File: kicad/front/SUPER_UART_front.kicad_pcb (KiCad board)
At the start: 2 copper layers, 100 x 43 mm, 253 parts, among them CON2 PIN-2x3, CON3 RS232, CON4 PORT D, CON5 PORT D, CON6 PORT B, CON7 PORT A, CON8 PORT C, Q1 PDTA143ZT, Q10 2N7002PS, Q11 N-MOS_small, Q12 PDTA143ZT, Q13 N-MOS_small, Q14 N-MOS_small, Q2 PDTA143ZT, Q3 N-MOS_small, Q4 PDTA143ZT, Q5 2N7002PS, Q6 N-MOS_small, Q7 PDTA143ZT, Q8 N-MOS_small, Q9 PDTA143ZT, SW1 5V_1, SW10 3V3_2, SW11 2V5_2, SW12 1V8_2, SW13 I2C_A, SW14 SPI_A, SW15 I2C_B, SW16 SPI_B, SW17 BOOT, SW18 DTR, SW19 RTS, SW2 3V3_1, SW3 2V5_1, SW4 1V8_1, SW5 RX, SW6 TX, SW7 SPY, SW8 ISO, SW9 5V_2, U1 STM32F030C6T6, U10 LP2951CD, U11 74HC595D, U12 74LVC8T245PW, U13 74LVC2T45DCU, U14 74LVC1T45GW, U15 74LVC1T45GW, U16 LP2951CD, U2 MIC5504-3.3YM5-TR, U4 74HC08P, U5 MAX3243EIPW, U6 74HC08P, U7 74LVC8T245PW, U8 74LVC8T245PW, U9 74LVC1T45GW

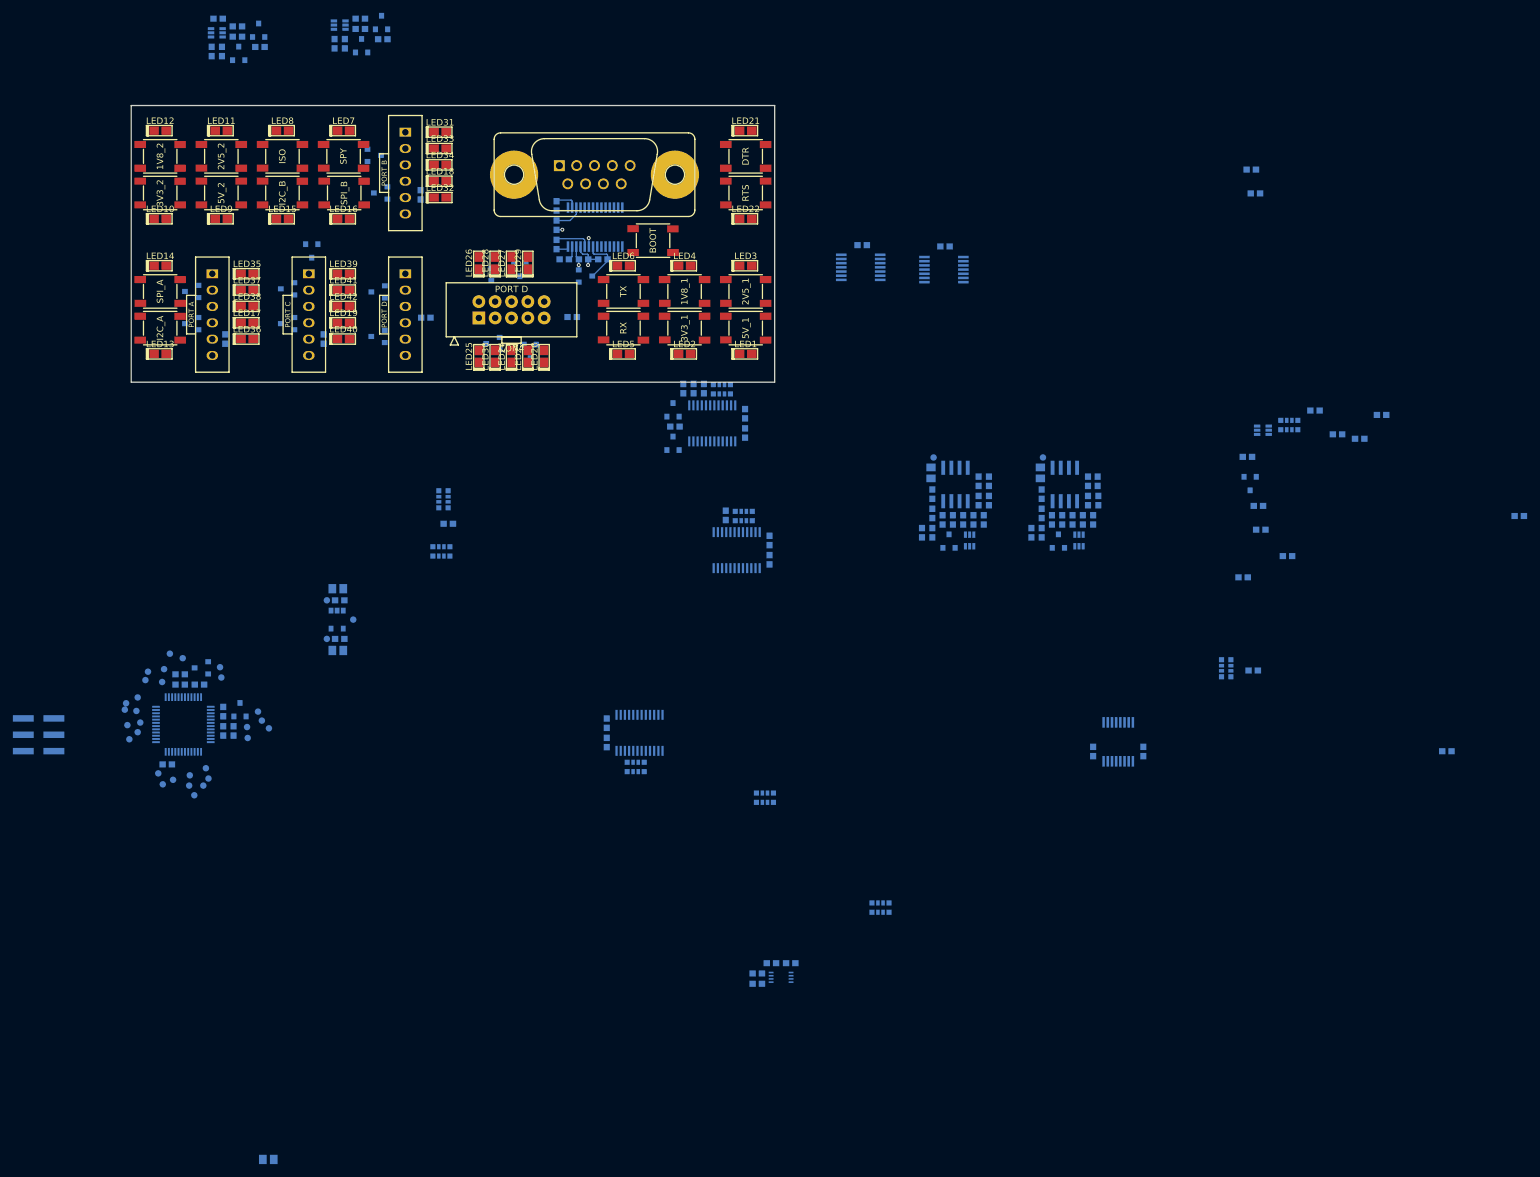
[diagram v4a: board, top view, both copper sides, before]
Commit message: Routing before moving to 4 layers
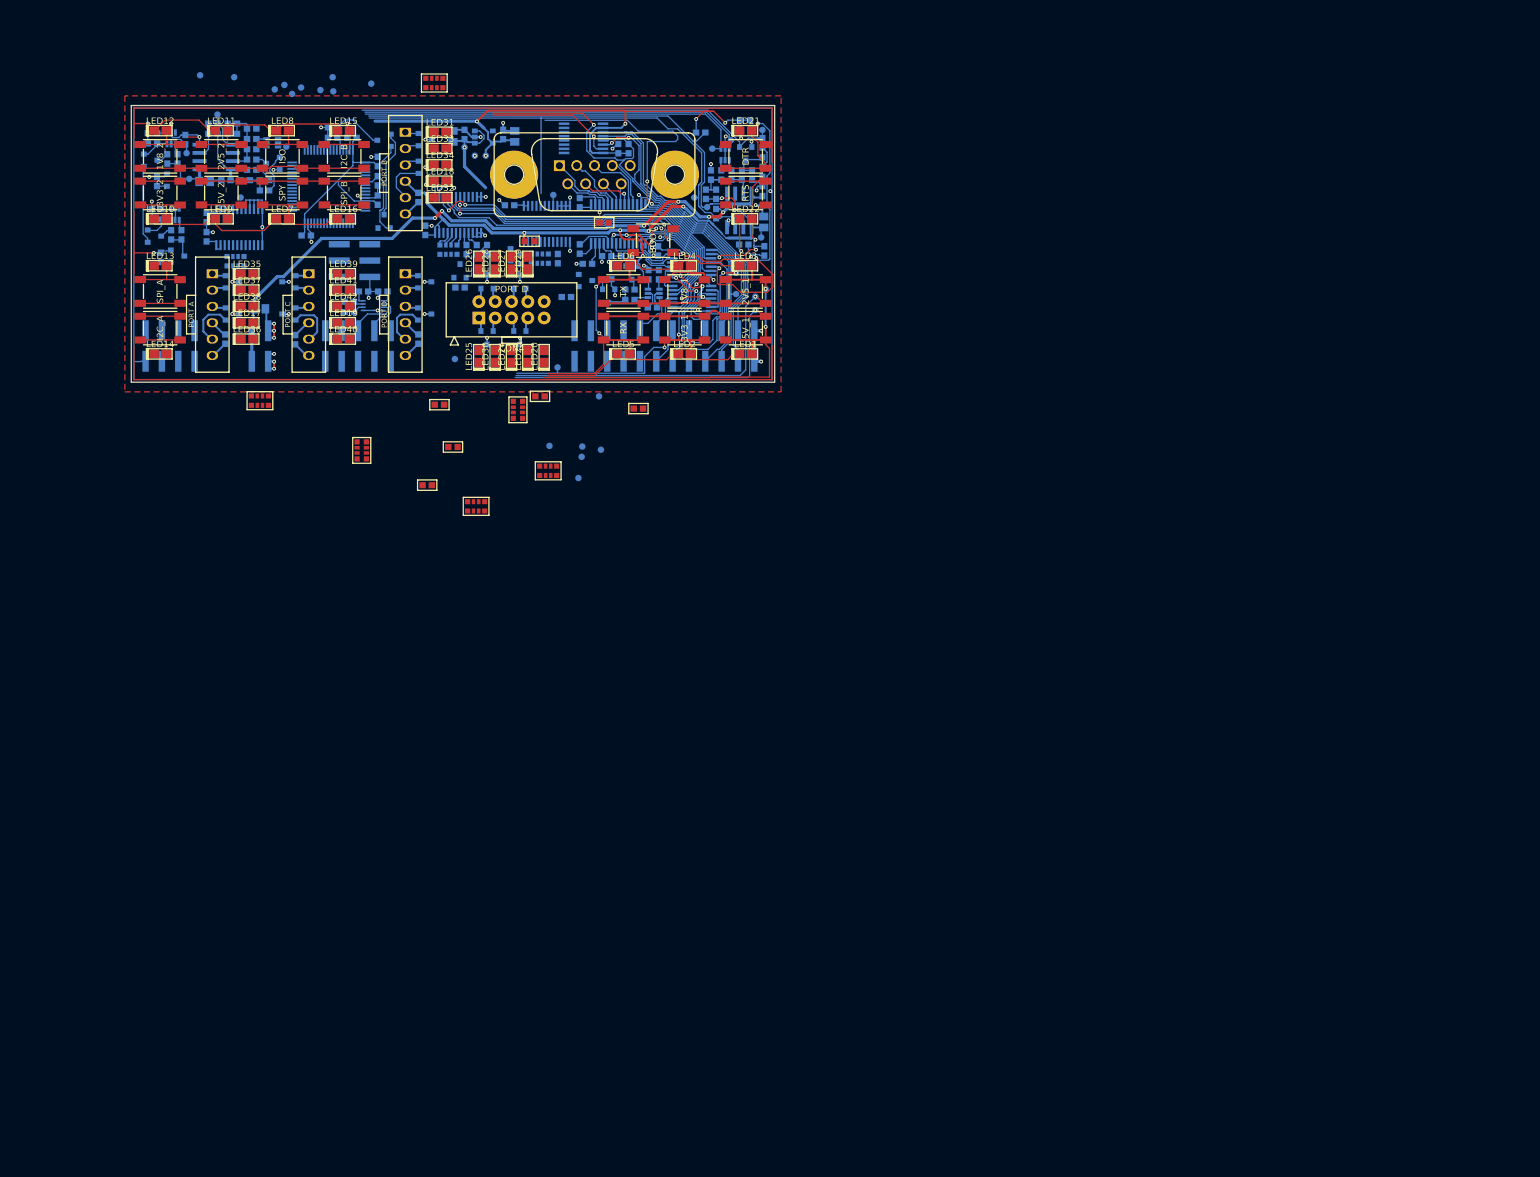
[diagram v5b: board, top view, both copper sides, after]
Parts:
- added CON1: PIN-2x4, pnPinheaders:PIN4x2SMD, B.Cu at (26.0, 55.9)
- added CON10: PIN-2x5, pnPinheaders:PIN5x2SMD, B.Cu at (55.2, 55.9)
- added CON11: PIN-2x12, pnPinheaders:PIN12x2SMD, B.Cu at (102.9, 55.9)
- added CON9: PIN-2x2, pnPinheaders:PIN2x2SMD, B.Cu at (40.0, 55.9)
- added TP36: Testpoint, pnConnector:TP_1mm, B.Cu at (42.3, 16.0)
- added TP37: Testpoint, pnConnector:TP_1mm, B.Cu at (43.8, 15.3)
- added TP38: Testpoint, pnConnector:TP_1mm, B.Cu at (45.0, 16.7)
- added TP39: Testpoint, pnConnector:TP_1mm, B.Cu at (51.4, 16.3)
- C15, C18, C21, R1, R14, R7, R8, RN1, RN2, RN3, RN6, RN8, RN9: moved to F.Cu
- U1: value STM32F030C6T6 -> STM32F030R8T6; footprint ST_LQFP48_ST_default -> niceSemiconductors:QFP-64-0.5_N
- moved R37 148.3 mm to (32.7, 21.3), turned to 180 degrees
- moved C43 146.8 mm to (35.7, 21.3), turned to 0 degrees
- moved R38 146.3 mm to (32.7, 22.9), turned to 0 degrees
- moved R40 144.7 mm to (35.7, 22.9), turned to 180 degrees
- moved R45 144.2 mm to (38.7, 22.1), turned to 180 degrees
- moved RN6 143.1 mm to (67.1, 15.0)
- moved R44 142.1 mm to (38.7, 23.7), turned to 180 degrees
- moved U16 141.4 mm to (33.2, 26.5), turned to 90 degrees
- moved C30 140.4 mm to (100.4, 44.8), turned to 90 degrees
- moved R43 140.0 mm to (38.7, 25.3), turned to 180 degrees
- moved Q10 139.8 mm to (41.9, 24.3), turned to 270 degrees
- moved TP35 139.6 mm to (29.0, 29.9), turned to 90 degrees
- moved R42 137.9 mm to (38.7, 26.9), turned to 180 degrees
- moved C44 137.6 mm to (31.4, 30.3), turned to 0 degrees
- moved R7 136.1 mm to (67.9, 65.0)
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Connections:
- net /CTS_A  renamed /CTS_A
- net /CTS_B  renamed /CTS_B
- net /CTS_C  renamed /CTS_C
- net /DTR_A  renamed /DTR_A
- net /DTR_B  renamed /DTR_B
- net /DTR_C  renamed /DTR_C
- net /RI_D  renamed /RI_D
- D10 pad 1: /SUPER_UART_front_UART234/DTR_A_VDD2 -> /SUPER_UART_front_UART234/RXD_A_VDD2
- D10 pad 2: /SUPER_UART_front_UART234/TXD_A_VDD2 -> /SUPER_UART_front_UART234/DTR_A_VDD2
- D11 pad 1: /SUPER_UART_front_UART234/RXD_A_VDD2 -> /SUPER_UART_front_UART234/CTS_A_VDD2
- D11 pad 2: /SUPER_UART_front_UART234/CTS_A_VDD2 -> /SUPER_UART_front_UART234/TXD_A_VDD2
- D12 pad 2: /SUPER_UART_front_UART234/TXD_C_VDD2 -> /SUPER_UART_front_UART234/RXD_C_VDD2
- D13 pad 1: /SUPER_UART_front_UART234/RXD_C_VDD2 -> /SUPER_UART_front_UART234/TXD_C_VDD2
- D6 pad 1: /SUPER_UART_front_UART1/DTR_D_VDD1 -> /SUPER_UART_front_UART1/CTS_D_VDD1
- D7 pad 2: /SUPER_UART_front_UART1/CTS_D_VDD1 -> /SUPER_UART_front_UART1/DTR_D_VDD1
- D8 pad 1: /SUPER_UART_front_UART1/DTR_B_VDD1 -> /SUPER_UART_front_UART1/CTS_B_VDD1
- D9 pad 2: /SUPER_UART_front_UART1/CTS_B_VDD1 -> /SUPER_UART_front_UART1/DTR_B_VDD1
- LED1 pad 1: /SUPER_UART_front_uC/COL1 -> /SUPER_UART_front_uC/COL3
- LED1 pad 2: /SUPER_UART_front_uC/LED1 -> /SUPER_UART_front_uC/LED2
- LED10 pad 1: /SUPER_UART_front_uC/COL2 -> /SUPER_UART_front_uC/COL4
- LED10 pad 2: /SUPER_UART_front_uC/LED3 -> /SUPER_UART_front_uC/LED4
- LED13 pad 1: /SUPER_UART_front_uC/COL1 -> /SUPER_UART_front_uC/COL4
- LED13 pad 2: /SUPER_UART_front_uC/LED4 -> /SUPER_UART_front_uC/LED1
- LED14 pad 1: /SUPER_UART_front_uC/COL2 -> /SUPER_UART_front_uC/COL4
- LED14 pad 2: /SUPER_UART_front_uC/LED4 -> /SUPER_UART_front_uC/LED2
- LED15 pad 1: /SUPER_UART_front_uC/COL3 -> /SUPER_UART_front_uC/COL1
- LED15 pad 2: /SUPER_UART_front_uC/LED4 -> /SUPER_UART_front_uC/LED3
- LED16 pad 1: /SUPER_UART_front_uC/COL4 -> /SUPER_UART_front_uC/COL1
- LED2 pad 2: /SUPER_UART_front_uC/LED1 -> /SUPER_UART_front_uC/LED2
- LED4 pad 1: /SUPER_UART_front_uC/COL4 -> /SUPER_UART_front_uC/COL2
- LED6 pad 1: /SUPER_UART_front_uC/COL2 -> /SUPER_UART_front_uC/COL1
- LED6 pad 2: /SUPER_UART_front_uC/LED2 -> /SUPER_UART_front_uC/LED1
- LED7 pad 1: /SUPER_UART_front_uC/COL3 -> /SUPER_UART_front_uC/COL2
- LED7 pad 2: /SUPER_UART_front_uC/LED2 -> /SUPER_UART_front_uC/LED4
- LED8 pad 1: /SUPER_UART_front_uC/COL4 -> /SUPER_UART_front_uC/COL2
- LED8 pad 2: /SUPER_UART_front_uC/LED2 -> /SUPER_UART_front_uC/LED3
- LED9 pad 1: /SUPER_UART_front_uC/COL1 -> /SUPER_UART_front_uC/COL3
- LED9 pad 2: /SUPER_UART_front_uC/LED3 -> /SUPER_UART_front_uC/LED4
- RN3 pad 5: /DCD_D  -> /DCD_D
- RN3 pad 6: /DSR_D  -> /DSR_D
- RN3 pad 7: /CTS_D  -> /CTS_D
- SW1 pad 1: /SUPER_UART_front_uC/SW1 -> /SUPER_UART_front_uC/SW2
- SW1 pad 2: /SUPER_UART_front_uC/COL1 -> /SUPER_UART_front_uC/COL3
- SW10 pad 1: /SUPER_UART_front_uC/SW3 -> /SUPER_UART_front_uC/SW4
- SW10 pad 2: /SUPER_UART_front_uC/COL2 -> /SUPER_UART_front_uC/COL4
- SW13 pad 1: /SUPER_UART_front_uC/SW4 -> /SUPER_UART_front_uC/SW1
- SW13 pad 2: /SUPER_UART_front_uC/COL1 -> /SUPER_UART_front_uC/COL4
- SW14 pad 1: /SUPER_UART_front_uC/SW4 -> /SUPER_UART_front_uC/SW2
- SW14 pad 2: /SUPER_UART_front_uC/COL2 -> /SUPER_UART_front_uC/COL4
- SW15 pad 1: /SUPER_UART_front_uC/SW4 -> /SUPER_UART_front_uC/SW3
- SW15 pad 2: /SUPER_UART_front_uC/COL3 -> /SUPER_UART_front_uC/COL1
- SW16 pad 2: /SUPER_UART_front_uC/COL4 -> /SUPER_UART_front_uC/COL1
- SW2 pad 1: /SUPER_UART_front_uC/SW1 -> /SUPER_UART_front_uC/SW2
- SW4 pad 2: /SUPER_UART_front_uC/COL4 -> /SUPER_UART_front_uC/COL2
- SW6 pad 1: /SUPER_UART_front_uC/SW2 -> /SUPER_UART_front_uC/SW1
- SW6 pad 2: /SUPER_UART_front_uC/COL2 -> /SUPER_UART_front_uC/COL1
- SW7 pad 1: /SUPER_UART_front_uC/SW2 -> /SUPER_UART_front_uC/SW4
- SW7 pad 2: /SUPER_UART_front_uC/COL3 -> /SUPER_UART_front_uC/COL2
- SW8 pad 1: /SUPER_UART_front_uC/SW2 -> /SUPER_UART_front_uC/SW3
- SW8 pad 2: /SUPER_UART_front_uC/COL4 -> /SUPER_UART_front_uC/COL2
- SW9 pad 1: /SUPER_UART_front_uC/SW3 -> /SUPER_UART_front_uC/SW4
- SW9 pad 2: /SUPER_UART_front_uC/COL1 -> /SUPER_UART_front_uC/COL3
- TP2 pad 1: /TXD_D  -> /TXD_D
- U1 pad 10: /~USB_SUSPEND -> /SUPER_UART_front_uC/COL3
- U1 pad 11: /~PWREN -> /SUPER_UART_front_uC/COL4
- U1 pad 12: /FTDI_RESET -> GND
- U1 pad 13: /SUPER_UART_front_UART1/~VDD1_ERR -> +3V3
- U1 pad 14: /CLPD_OE -> /~USB_SUSPEND
- U1 pad 15: /CPLD_BOOT_EN -> /~PWREN
- U1 pad 16: /SUPER_UART_front_uC/LED1uC -> /FTDI_RESET
- U1 pad 17: /SUPER_UART_front_uC/LED2uC -> /SUPER_UART_front_UART1/~VDD1_ERR
- U1 pad 18: /SUPER_UART_front_uC/LED3uC -> (no net)
- U1 pad 19: /SUPER_UART_front_uC/LED4uC -> (no net)
- U1 pad 2: /SUPER_UART_front_UART234/I2C_PU_EN_A -> /AUX3
- U1 pad 20: /SUPER_UART_front_RS232/~VDD1_EN -> /CLPD_OE
- U1 pad 21: /SUPER_UART_front_UART1/I2C_PU_EN_B -> /CPLD_BOOT_EN
- U1 pad 22: /SUPER_UART_front_UART1/SPI_EN_B -> /SUPER_UART_front_uC/LED1uC
- U1 pad 23: GND -> /SUPER_UART_front_uC/LED2uC
- U1 pad 24: +3V3 -> /SUPER_UART_front_uC/SW1
- U1 pad 25: /SR_LOAD -> /SUPER_UART_front_uC/SW2
- U1 pad 26: /SR_CLK -> /SUPER_UART_front_uC/LED3uC
- U1 pad 27: /SUPER_UART_front_uC/COL4 -> /SUPER_UART_front_uC/LED4uC
- U1 pad 28: /SR_DATA -> /SUPER_UART_front_RS232/~VDD1_EN
- U1 pad 29: /SUPER_UART_front_uC/LED5uC -> /SUPER_UART_front_UART1/I2C_PU_EN_B
- U1 pad 3: /SUPER_UART_front_UART234/SPI_EN_A -> (no net)
- U1 pad 30: /SUPER_UART_front_RS232/RXD_D3 -> /SUPER_UART_front_UART1/SPI_EN_B
- U1 pad 31: /TXD_D  -> GND
- U1 pad 32: /SUPER_UART_front_uC/SW2 -> +3V3
- U1 pad 33: /SUPER_UART_front_uC/SW3 -> /SR_LOAD
- U1 pad 34: /SUPER_UART_front_uC/SWDIO -> /SR_CLK
- U1 pad 35: /SUPER_UART_front_uC/COL3 -> (no net)
- U1 pad 36: /SUPER_UART_front_uC/COL2 -> /SR_DATA
- U1 pad 37: /SUPER_UART_front_uC/SWDCLK -> /SUPER_UART_front_uC/SW3
- U1 pad 39: /SUPER_UART_front_UART1/VDD1_SEL1 -> /SUPER_UART_front_UART234/I2C_PU_EN_A
- U1 pad 4: /SUPER_UART_front_uC/COL1 -> (no net)
- U1 pad 40: /SUPER_UART_front_UART1/VDD1_SEL2 -> /SUPER_UART_front_UART234/SPI_EN_A
- U1 pad 41: /SUPER_UART_front_UART1/VDD1_SEL3 -> /SUPER_UART_front_uC/LED5uC
- U1 pad 42: /SUPER_UART_front_UART234/~VDD2_EN -> /SUPER_UART_front_RS232/RXD_D3
- U1 pad 43: /SUPER_UART_front_UART234/VDD2_SEL1 -> /TXD_D
- U1 pad 44: /SUPER_UART_front_uC/BOOT0 -> Net-(TP36-Pad1)
- U1 pad 45: /SUPER_UART_front_UART234/VDD2_SEL2 -> Net-(TP37-Pad1)
- U1 pad 46: /SUPER_UART_front_UART234/VDD2_SEL3 -> /SUPER_UART_front_uC/SWDIO
- U1 pad 47: GND -> (no net)
- U1 pad 48: +3V3 -> (no net)
- U1 pad 5: /SUPER_UART_front_uC/SW1 -> (no net)
- U1 pad 6: /SUPER_UART_front_UART234/~VDD2_ERR -> (no net)
- U1 pad 8: GND -> /SUPER_UART_front_uC/COL1
- U1 pad 9: +3V3 -> /SUPER_UART_front_uC/COL2
- U11 pad 11: /EECLK  -> /EECLK
- U11 pad 12: /EECS  -> /EECS
- U11 pad 14: /EEDATA  -> /EEDATA
- U12 pad 22: (no net) -> /SUPER_UART_front_UART234/~VDD2_EN
- U12 pad 3: /TXD_A  -> /TXD_A
- U12 pad 5: /TXD_C  -> /TXD_C
- U13 pad 2: /RXD_C  -> /RXD_C
- U15 pad 3: /RXD_A  -> /RXD_A
- U4 pad 1: /DTR_D  -> /RTS_D
- U4 pad 10: /SUPER_UART_front_RS232/DSR_D2 -> /SUPER_UART_front_RS232/DCD_D2
- U4 pad 11: /DCD_D  -> /CTS_D
- U4 pad 12: /SUPER_UART_front_RS232/DCD_D1 -> /SUPER_UART_front_RS232/CTS_D2
- U4 pad 13: /SUPER_UART_front_RS232/DCD_D2 -> /SUPER_UART_front_RS232/CTS_D1
- U4 pad 2: /SUPER_UART_front_RS232/DTR_FORCE -> /SUPER_UART_front_RS232/RTS_FORCE
- U4 pad 3: /SUPER_UART_front_RS232/DTR_D1 -> /SUPER_UART_front_RS232/RTS_D1
- U4 pad 4: /RTS_D  -> /DTR_D
- U4 pad 5: /SUPER_UART_front_RS232/RTS_FORCE -> /SUPER_UART_front_RS232/DTR_FORCE
- U4 pad 6: /SUPER_UART_front_RS232/RTS_D1 -> /SUPER_UART_front_RS232/DTR_D1
- U4 pad 8: /DSR_D  -> /DCD_D
- U4 pad 9: /SUPER_UART_front_RS232/DSR_D1 -> /SUPER_UART_front_RS232/DCD_D1
- U5 pad 13: /TXD_D  -> /TXD_D
- U6 pad 10: /SUPER_UART_front_RS232/RXD_D3 -> /SUPER_UART_front_RS232/DSR_D2
- U6 pad 3: /RXD_D  -> /RXD_D
- U6 pad 4: (no net) -> /SUPER_UART_front_RS232/RXD_D2
- U6 pad 5: /SUPER_UART_front_RS232/CTS_D2 -> /SUPER_UART_front_RS232/RXD_D3
- U6 pad 6: /CTS_D  -> Net-(U6-Pad2)
- U6 pad 8: Net-(U6-Pad2) -> /DSR_D
- U6 pad 9: /SUPER_UART_front_RS232/RXD_D2 -> /SUPER_UART_front_RS232/DSR_D1
- U7 pad 22: (no net) -> /SUPER_UART_front_RS232/~VDD1_EN
- U7 pad 3: /TXD_D  -> /TXD_D
- U7 pad 4: /SUPER_UART_front_RS232/~VDD1_EN -> /SUPER_UART_front_RS232/DTR_D1
- U7 pad 6: /TXD_B  -> /TXD_B
- U8 pad 22: (no net) -> GND
- U8 pad 4: GND -> /SUPER_UART_front_RS232/CTS_D1
- U8 pad 8: /RXD_B  -> /RXD_B
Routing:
- net GND: track 6.27 -> 591.9 mm, vias 2 -> 62
- net +3V3: track 5.14 -> 184.3 mm, vias 2 -> 12
- net +5V: track 0.00 -> 128.9 mm, vias 0 -> 7
- net (no net): track 0.00 -> 109.8 mm
- net VDD1: track 0.00 -> 105.8 mm, vias 0 -> 7
- net /SUPER_UART_front_uC/COL3: track 0.00 -> 84.0 mm, vias 0 -> 2
- net /SUPER_UART_front_RS232/~VDD1_EN: track 0.00 -> 83.3 mm
- net /SUPER_UART_front_uC/SW1: track 0.00 -> 81.6 mm, vias 0 -> 1
- net /SUPER_UART_front_uC/SW2: track 0.00 -> 81.2 mm, vias 0 -> 1
- net /~PWREN: track 0.00 -> 80.0 mm, vias 0 -> 1
- net /SUPER_UART_front_uC/COL2: track 0.00 -> 73.9 mm, vias 0 -> 3
- net /SUPER_UART_front_RS232/RXD_D3: track 0.00 -> 71.7 mm, vias 0 -> 4
- net /SUPER_UART_front_UART1/~VDD1_ERR: track 0.00 -> 71.4 mm
- net /SUPER_UART_front_UART1/VDD1_SEL1: track 0.00 -> 66.9 mm
- net /SUPER_UART_front_UART1/VDD1_SEL2: track 0.00 -> 61.2 mm
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- added copper zone on F.Cu, net GND

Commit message: Front board routed
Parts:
- removed C18: 100n, 0603_N
- R1, R14, R7, R8, RN1, RN2, RN3, RN6, RN8, RN9: moved to B.Cu
- moved TP13 74.9 mm to (23.0, 42.0)
- moved TP15 71.4 mm to (41.1, 21.1)
- moved TP16 69.4 mm to (30.4, 36.2)
- moved TP14 51.0 mm to (50.0, 44.5)
- moved RN9 41.0 mm to (62.4, 40.9), turned to 180 degrees
- moved R1 40.8 mm to (45.9, 42.0), turned to 270 degrees
- moved RN2 37.1 mm to (90.3, 47.7), turned to 180 degrees
- moved TP20 33.5 mm to (23.4, 32.6)
- moved R8 33.1 mm to (71.5, 47.0)
- moved RN1 30.7 mm to (49.7, 42.0), turned to 180 degrees
- moved TP21 23.1 mm to (21.5, 32.1)
- moved RN8 22.6 mm to (43.1, 42.0), turned to 0 degrees
- moved R7 19.9 mm to (71.5, 45.4)
- moved TP9 19.7 mm to (30.6, 22.1)
- moved RN6 18.4 mm to (83.3, 23.8), turned to 90 degrees
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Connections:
- RN5 pad 1: /SUPER_UART_front_UART1/DSR_D_VDD1 -> /SUPER_UART_front_UART1/DCD_D_VDD1
- RN5 pad 2: /SUPER_UART_front_UART1/DCD_D_VDD1 -> /SUPER_UART_front_UART1/DSR_D_VDD1
- RN6 pad 2: Net-(LED34-Pad2) -> Net-(LED33-Pad2)
- RN6 pad 3: Net-(LED33-Pad2) -> Net-(LED34-Pad2)
- RN6 pad 6: /SUPER_UART_front_UART1/TXD_B_LED -> /SUPER_UART_front_UART1/RXD_B_LED
- RN6 pad 7: /SUPER_UART_front_UART1/RXD_B_LED -> /SUPER_UART_front_UART1/TXD_B_LED
- RN7 pad 3: /SUPER_UART_front_UART234/DTR_A_VDD2 -> /SUPER_UART_front_UART234/TXD_A_VDD2
- RN7 pad 4: /SUPER_UART_front_UART234/TXD_A_VDD2 -> /SUPER_UART_front_UART234/DTR_A_VDD2
- TP13 pad 1: /SUPER_UART_front_uC/LED1uC -> /SUPER_UART_front_uC/LED1
- TP14 pad 1: /SUPER_UART_front_uC/LED2uC -> /SUPER_UART_front_uC/LED2
- TP15 pad 1: /SUPER_UART_front_uC/LED3uC -> /SUPER_UART_front_uC/LED3
- TP16 pad 1: /SUPER_UART_front_uC/LED4uC -> /SUPER_UART_front_uC/LED4
- TP17 pad 1: /SUPER_UART_front_uC/LED5uC -> /SUPER_UART_front_uC/LED5
- U1 pad 10: /SUPER_UART_front_uC/COL3 -> /SUPER_UART_front_UART1/SPI_EN_B
- U1 pad 11: /SUPER_UART_front_uC/COL4 -> /~USB_SUSPEND
- U1 pad 14: /~USB_SUSPEND -> /SUPER_UART_front_RS232/~VDD1_EN
- U1 pad 15: /~PWREN -> /SUPER_UART_front_uC/SW3
- U1 pad 17: /SUPER_UART_front_UART1/~VDD1_ERR -> (no net)
- U1 pad 2: /AUX3 -> /~PWREN
- U1 pad 20: /CLPD_OE -> (no net)
- U1 pad 25: /SUPER_UART_front_uC/SW2 -> (no net)
- U1 pad 28: /SUPER_UART_front_RS232/~VDD1_EN -> (no net)
- U1 pad 29: /SUPER_UART_front_UART1/I2C_PU_EN_B -> /AUX1
- U1 pad 30: /SUPER_UART_front_UART1/SPI_EN_B -> /AUX3
- U1 pad 37: /SUPER_UART_front_uC/SW3 -> /AUX2
- U1 pad 38: /SUPER_UART_front_uC/SW4 -> /SUPER_UART_front_uC/COL3
- U1 pad 39: /SUPER_UART_front_UART234/I2C_PU_EN_A -> /SUPER_UART_front_uC/COL4
- U1 pad 4: (no net) -> /SUPER_UART_front_uC/COL2
- U1 pad 40: /SUPER_UART_front_UART234/SPI_EN_A -> /SUPER_UART_front_UART234/I2C_PU_EN_A
- U1 pad 44: Net-(TP36-Pad1) -> /SUPER_UART_front_UART1/VDD1_SEL1
- U1 pad 45: Net-(TP37-Pad1) -> /SUPER_UART_front_uC/SW4
- U1 pad 47: (no net) -> /SUPER_UART_front_UART1/VDD1_SEL2
- U1 pad 48: (no net) -> /SUPER_UART_front_UART1/VDD1_SEL3
- U1 pad 5: (no net) -> /SUPER_UART_front_UART1/I2C_PU_EN_B
- U1 pad 51: /SUPER_UART_front_UART234/~VDD2_ERR -> Net-(TP37-Pad1)
- U1 pad 52: /AUX1 -> Net-(TP36-Pad1)
- U1 pad 53: /AUX2 -> /SUPER_UART_front_UART234/VDD2_SEL3
- U1 pad 55: /SUPER_UART_front_UART1/VDD1_SEL1 -> /SUPER_UART_front_UART234/VDD2_SEL2
- U1 pad 56: /SUPER_UART_front_UART1/VDD1_SEL2 -> /SUPER_UART_front_UART234/VDD2_SEL1
- U1 pad 57: /SUPER_UART_front_UART1/VDD1_SEL3 -> /SUPER_UART_front_UART234/SPI_EN_A
- U1 pad 59: /SUPER_UART_front_UART234/VDD2_SEL1 -> /SUPER_UART_front_UART234/~VDD2_ERR
- U1 pad 6: (no net) -> /SUPER_UART_front_UART1/~VDD1_ERR
- U1 pad 61: /SUPER_UART_front_UART234/VDD2_SEL2 -> /SUPER_UART_front_uC/COL1
- U1 pad 62: /SUPER_UART_front_UART234/VDD2_SEL3 -> (no net)
- U1 pad 8: /SUPER_UART_front_uC/COL1 -> /SUPER_UART_front_uC/SW2
- U1 pad 9: /SUPER_UART_front_uC/COL2 -> /CLPD_OE
- U12 pad 3: /TXD_A -> /DTR_A
- U12 pad 4: /DTR_A -> /TXD_A
- U8 pad 5: /SUPER_UART_front_RS232/DCD_D1 -> /SUPER_UART_front_RS232/DSR_D1
- U8 pad 6: /SUPER_UART_front_RS232/DSR_D1 -> /SUPER_UART_front_RS232/DCD_D1
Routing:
- net GND: track 591.9 -> 1294.4 mm, vias 62 -> 129
- net +3V3: track 184.3 -> 428.7 mm, vias 12 -> 21
- net /SUPER_UART_front_uC/COL4: track 33.5 -> 166.8 mm, vias 0 -> 11
- net (no net): track 109.8 -> 0.00 mm
- net /SUPER_UART_front_uC/LED5: track 0.00 -> 102.3 mm, vias 0 -> 5
- net /SUPER_UART_front_uC/SW4: track 31.5 -> 127.9 mm, vias 0 -> 6
- net /SUPER_UART_front_uC/LED1: track 21.3 -> 112.4 mm, vias 0 -> 2
- net /SUPER_UART_front_uC/COL1: track 56.8 -> 146.4 mm, vias 2 -> 9
- net /SUPER_UART_front_uC/COL3: track 84.0 -> 172.3 mm, vias 2 -> 8
- net /TXD_D: track 35.1 -> 122.1 mm, vias 1 -> 4
- net VDD2: track 26.4 -> 112.7 mm, vias 0 -> 10
- net /SR_CLK: track 0.00 -> 84.4 mm, vias 0 -> 3
- net /SUPER_UART_front_UART1/SPI_EN_B: track 3.12 -> 86.5 mm, vias 0 -> 4
- net /SUPER_UART_front_uC/LED2: track 32.7 -> 115.3 mm, vias 0 -> 2
- net /SUPER_UART_front_uC/COL2: track 73.9 -> 150.7 mm, vias 3 -> 9
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- added copper zone on B.Cu, net +3V3
- added copper zone on F.Cu, net +3V3
- added copper zone on In1.Cu, net +3V3
- added copper zone on F.Cu, net +5V
- added copper zone on In1.Cu, net +5V
- added copper zone on B.Cu, net GND
- added copper zone on In1.Cu, net GND
- added copper zone on In2.Cu, net GND
- added copper zone on F.Cu, net VDD1
- added copper zone on In1.Cu, net VDD1
- added copper zone on F.Cu, net VDD2
- added copper zone on In1.Cu, net VDD2
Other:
- copper layers 2 -> 4
- net class Default: clearance 0.1524 -> 0.17
- net class IO added: clearance 0.25, trace_width 0.1524, via_dia 0.6048, via_drill 0.3
- rule trace_clearance: 0.1524 -> 0.17
- board text added: "1"
- board text added: "2"
- board text added: "3"
- board text added: "4"
